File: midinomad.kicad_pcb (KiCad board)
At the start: 2 copper layers, 169.1 x 87.3 mm, 56 parts, among them J1 MIDI IN, J2 MIDI OUT, J3 Nomad 45, 55, J7 DC IN, U1 6N138, U2 L7805, U3 74HC4053

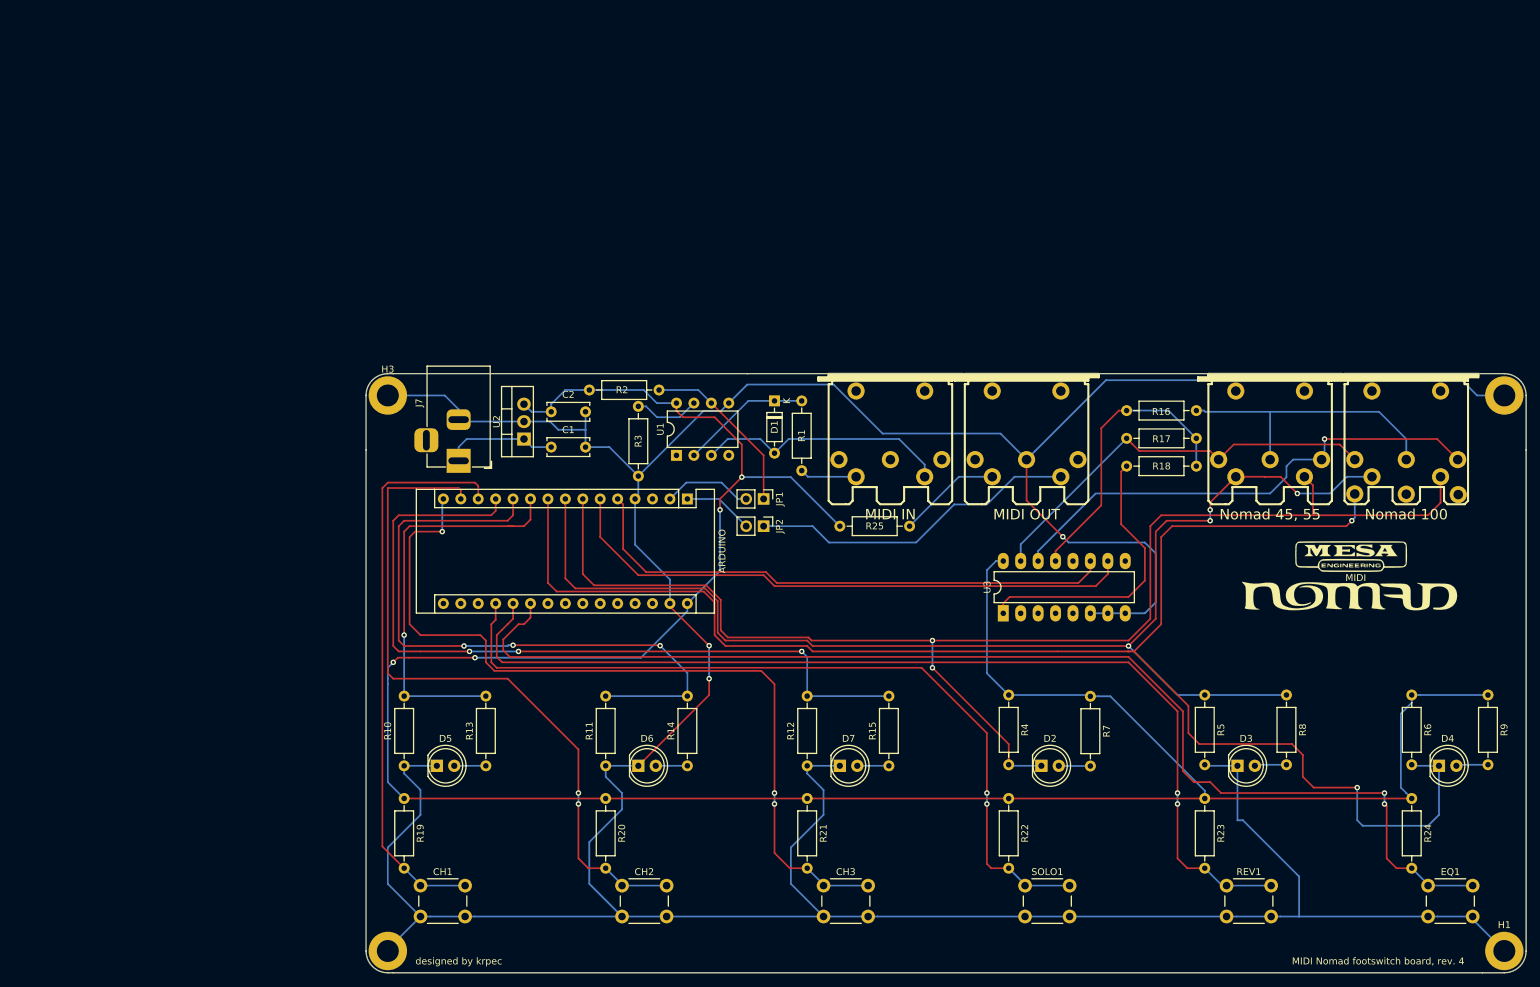
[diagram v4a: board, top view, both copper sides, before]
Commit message: Updated both schematics & PCB, added second 74hc4053.
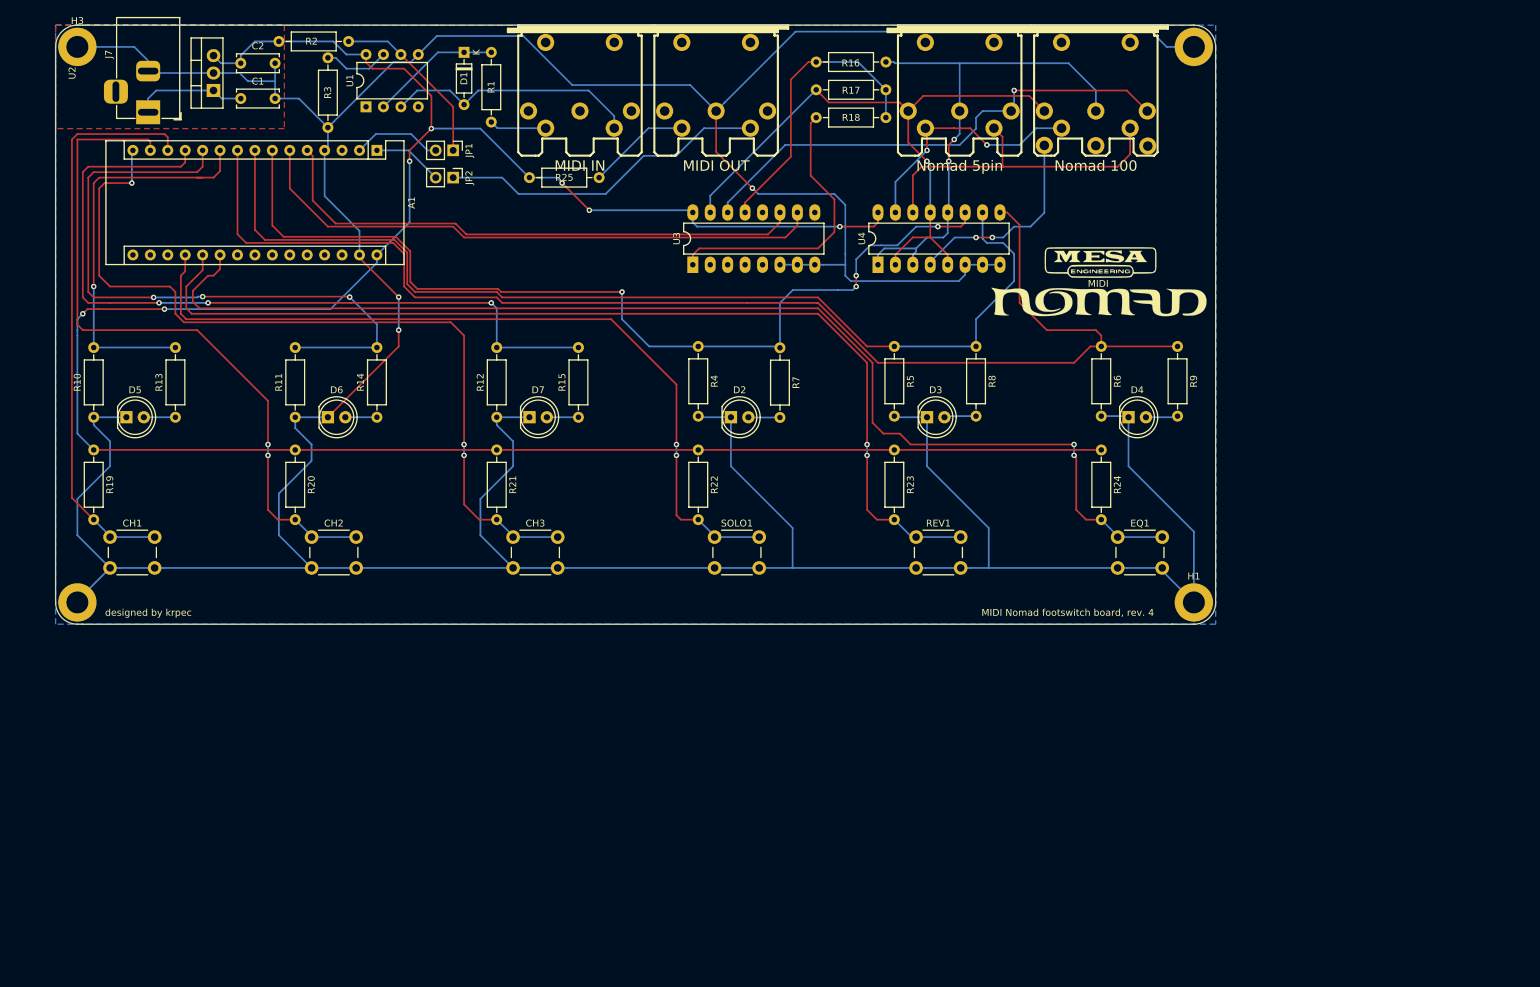
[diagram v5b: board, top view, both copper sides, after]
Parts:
- removed ARDUINO: Arduino_Nano_v3.x, Module:Arduino_Nano
- removed the G*** at (208.8, 101.6)
- removed NOMAD 100: Nomad 100, midinomad:din-8
- added A1: Arduino_Nano_v3.x, Module:Arduino_Nano, F.Cu at (66.7, 40.5)
- added G***: LOGO, midinomad-mux:board-logo, F.Cu at (172.2, 58.7)
- added J4: Nomad 100, midinomad:din-8, F.Cu at (171.4, 31.8)
- added U4: 74HC4053, Package_DIP:DIP-16_W7.62mm_LongPads, F.Cu at (139.7, 57.1)
- J3: value Nomad 45, 55 -> Nomad 5pin
- moved D1 68.0 mm to (79.4, 26.2)
- moved D2 68.0 mm to (118.3, 79.4)
- moved D3 68.0 mm to (146.8, 79.4)
- moved D4 68.0 mm to (176.2, 79.4)
- moved D5 68.0 mm to (30.2, 79.4)
- moved D6 68.0 mm to (59.5, 79.4)
- moved D7 68.0 mm to (88.9, 79.4)
- moved H3 68.0 mm to (23.0, 25.4)
- moved R1 68.0 mm to (83.3, 26.2)
- moved R10 68.0 mm to (25.4, 79.4)
- moved R11 68.0 mm to (54.8, 79.4)
- moved R12 68.0 mm to (84.1, 79.4)
- moved R13 68.0 mm to (37.3, 79.4)
- moved R14 68.0 mm to (66.7, 79.4)
- moved R15 68.0 mm to (96.0, 79.4)
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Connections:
- D2 pad 1: Arduino_D4 -> GNDREF
- D4 pad 1: Arduino_D6 -> GNDREF
- J3 pad 4: Arduino_D5 -> MESA_SWB_(REV)
- J3 pad 5: Arduino_D4 -> MESA_SWA_(SOLO)
- R4 pad 1: +5V -> Arduino_D4
- R4 pad 2: Arduino_D4 -> GNDREF
- R6 pad 1: +5V -> Arduino_D6
- R6 pad 2: Arduino_D6 -> GNDREF
- R7 pad 1: +5V -> Arduino_D4
- R9 pad 1: +5V -> Arduino_D6
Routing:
- net GNDREF: track 578.0 -> 670.5 mm
- net Arduino_D4: track 196.3 -> 139.4 mm, vias 2 -> 4
- net MESA_SWA_(SOLO): track 0.00 -> 48.3 mm
- net Arduino_D6: track 229.7 -> 191.4 mm, vias 2 -> 0
- net MESA_SWB_(REV): track 0.00 -> 36.1 mm, vias 0 -> 2
- net +2V: track 42.3 -> 76.3 mm, vias 0 -> 2
- net -3V: track 60.6 -> 93.0 mm, vias 0 -> 1
- net Arduino_D5: track 183.1 -> 151.5 mm, vias 4 -> 0
- net +5V: track 383.2 -> 353.2 mm, vias 4 -> 7
- net MESA_SWC_(EQ): track 0.00 -> 29.8 mm, vias 0 -> 2
- added copper zone on B.Cu, net GNDREF
- added copper zone on F.Cu, net GNDREF

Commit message: schematics changes
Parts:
- removed G***: LOGO, midinomad-mux:board-logo
- added C3: 0.1uF, Capacitor_THT:C_Disc_D6.0mm_W2.5mm_P5.00mm, F.Cu at (74.6, 48.4)
- added C4: 0.1uF, Capacitor_THT:C_Disc_D6.0mm_W2.5mm_P5.00mm, F.Cu at (108.7, 50.8)
- added C5: 0.1uF, Capacitor_THT:C_Disc_D6.0mm_W2.5mm_P5.00mm, F.Cu at (136.5, 49.8)
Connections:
- J7 pad 1: Net-(C1-Pad1) -> GNDREF
- J7 pad 2: GNDREF -> Net-(C1-Pad1)
- U4 pad 3: +2V -> -3V
- U4 pad 5: -3V -> +2V
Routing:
- net GNDREF: track 670.5 -> 712.6 mm
- net +2V: track 76.3 -> 87.7 mm
- net +5V: track 353.2 -> 361.3 mm
- net -3V: track 93.0 -> 90.5 mm
- net Net-(C1-Pad1): track 16.5 -> 17.1 mm

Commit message: Rev. 6 PCB & schematics
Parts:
- removed C4, C5: 0.1uF, Capacitor_THT:C_Disc_D6.0mm_W2.5mm_P5.00mm
- removed the U4 at (139.7, 57.1)
- added D10: LED, LED_THT:LED_D5.0mm, F.Cu at (220.7, 111.1)
- added D2: 1N4007, Diode_THT:D_DO-41_SOD81_P10.16mm_Horizontal, F.Cu at (169.9, 96.0)
- added D3: 1N4007, Diode_THT:D_DO-41_SOD81_P10.16mm_Horizontal, F.Cu at (194.5, 96.0)
- added G***: LOGO, midinomad-mux:board-logo, F.Cu at (122.2, 89.7)
- added K1: SANYOU_SRD_Form_C, Relay_THT:Relay_SPDT_SANYOU_SRD_Series_Form_C, F.Cu at (174.6, 92.1)
- added K2: SANYOU_SRD_Form_C, Relay_THT:Relay_SPDT_SANYOU_SRD_Series_Form_C, F.Cu at (199.2, 92.1)
- added K3: SANYOU_SRD_Form_C, Relay_THT:Relay_SPDT_SANYOU_SRD_Series_Form_C, F.Cu at (223.8, 92.1)
- added Q1: 2N2222, Package_TO_SOT_THT:TO-18-3, F.Cu at (162.7, 94.5)
- added Q2: 2N2222, Package_TO_SOT_THT:TO-18-3, F.Cu at (211.9, 94.5)
- added Q3: 2N2222, Package_TO_SOT_THT:TO-18-3, F.Cu at (187.3, 94.5)
- added R12: 220R, Resistor_THT:R_Axial_DIN0207_L6.3mm_D2.5mm_P10.16mm_Horizontal, F.Cu at (129.4, 77.8)
- added R2: 1k, Resistor_THT:R_Axial_DIN0207_L6.3mm_D2.5mm_P10.16mm_Horizontal, F.Cu at (154.8, 100.8)
- added R27: 10k, Resistor_THT:R_Axial_DIN0207_L6.3mm_D2.5mm_P10.16mm_Horizontal, F.Cu at (216.7, 100.8)
- added R28: 220R, Resistor_THT:R_Axial_DIN0207_L6.3mm_D2.5mm_P10.16mm_Horizontal, F.Cu at (227.8, 100.8)
- added R8: 1k, Resistor_THT:R_Axial_DIN0207_L6.3mm_D2.5mm_P10.16mm_Horizontal, F.Cu at (183.4, 100.8)
- added REF**: Symbol_GNU-GPL_CopperTop_Small, Symbol:Symbol_GNU-GPL_CopperTop_Small, F.Cu at (149.2, 131.8)
- added REF**: Polarity_Center_Negative_6mm_SilkScreen, Symbol:Polarity_Center_Negative_6mm_SilkScreen, F.Cu at (67.7, 66.5)
- added REF**: OSHW-Logo2_7.3x6mm_SilkScreen, Symbol:OSHW-Logo2_7.3x6mm_SilkScreen, F.Cu at (73.8, 131.8)
- added U2: MOC3041M, Package_DIP:DIP-6_W7.62mm_LongPads, F.Cu at (137.3, 74.6)
- D4: value LED -> 1N4007; footprint LED_THT:LED_D5.0mm -> Diode_THT:D_DO-41_SOD81_P10.16mm_Horizontal
- R6: value 10k -> 1k
- U3: value 74HC4053 -> MOC3041M; footprint Package_DIP:DIP-16_W7.62mm_LongPads -> Package_DIP:DIP-6_W7.62mm_LongPads
- moved R13 65.6 mm to (81.0, 119.1), turned to 180 degrees
- moved R14 65.6 mm to (169.1, 119.1), turned to 180 degrees
- moved R17 65.6 mm to (110.3, 119.1), turned to 180 degrees
- moved R18 65.6 mm to (197.6, 119.1), turned to 180 degrees
- moved R23 65.6 mm to (139.7, 119.1), turned to 180 degrees
- moved R24 65.0 mm to (227.0, 119.1), turned to 180 degrees
- moved R15 54.6 mm to (158.0, 100.8)
- moved R16 54.6 mm to (169.9, 101.0)
- moved D5 54.6 mm to (162.7, 111.1)
- moved D8 54.6 mm to (104.0, 111.1)
- moved R25 54.6 mm to (111.1, 111.1)
- moved R26 54.6 mm to (99.2, 111.1)
- moved R29 54.6 mm to (140.5, 111.1)
- moved R30 54.6 mm to (128.6, 111.1)
- moved D6 54.6 mm to (74.6, 111.1)
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- renumbered D2 to D5, D5 to D6, D3 to D7, D6 to D8, D7 to D9, J3 to J2, J4 to J3, J2 to J4, J7 to J5, R17 to R10, R18 to R11, R19 to R13, R22 to R14, R4 to R15, R7 to R16, R20 to R17, R23 to R18, R13 to R19, R10 to R20, R5 to R21, R8 to R22, R21 to R23, R14 to R25, R11 to R26, R15 to R29, R2 to R3, R12 to R30, R3 to R4, R25 to R5, R16 to R7, JP1 to RXJ1, JP2 to TXJ1, U2 to U4
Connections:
- D4 pad 1: GNDREF -> +5V
- R10 pad 2: Net-(R16-Pad1) -> Net-(R10-Pad2)
- R11 pad 1: Net-(R18-Pad1) -> Net-(R11-Pad1)
- R11 pad 2: Net-(R16-Pad1) -> Net-(R10-Pad2)
- R6 pad 1: Arduino_D6 -> Net-(Q2-Pad2)
- R6 pad 2: GNDREF -> Arduino_D6
- R7 pad 1: Net-(R16-Pad1) -> Net-(R10-Pad2)
- R9 pad 1: Arduino_D6 -> Net-(R9-Pad1)
- R9 pad 2: Net-(D4-Pad2) -> Arduino_D2
- U3 pad 1: Net-(R18-Pad1) -> Net-(R12-Pad1)
- U3 pad 2: Net-(U3-Pad2) -> GNDREF
- U3 pad 4: Net-(U3-Pad4) -> -3V
- U3 pad 6: GNDREF -> Net-(R11-Pad1)
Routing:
- net GNDREF: track 712.6 -> 520.5 mm, vias 3 -> 0
- net +5V: track 361.3 -> 417.4 mm, vias 7 -> 9
- net Arduino_D3: track 85.1 -> 29.9 mm
- net Arduino_D2: track 80.0 -> 26.2 mm
- net Net-(R10-Pad2): track 0.00 -> 52.3 mm
- net Net-(R16-Pad1): track 42.8 -> 0.00 mm
- net Net-(R18-Pad1): track 41.9 -> 0.00 mm
- net -3V: track 90.5 -> 53.0 mm, vias 1 -> 0
- net Net-(R11-Pad1): track 0.00 -> 37.0 mm
- net Net-(D2-Pad2): track 0.00 -> 26.0 mm
- net Net-(D3-Pad2): track 0.00 -> 26.0 mm
- net MESA_SWA_(SOLO): track 48.3 -> 73.4 mm, vias 0 -> 2
- net Net-(D4-Pad2): track 4.89 -> 26.1 mm
- net MESA_VCH: track 73.0 -> 94.1 mm, vias 1 -> 0
- net MESA_SWB_(REV): track 36.1 -> 55.9 mm, vias 2 -> 1
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- added copper zone on B.Cu, net -3V
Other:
- board text added: "MIDI Nomad footswitch board, rev. 6 | github.com/krpec/MIDINomad"
- board text removed: "MIDI Nomad footswitch board, rev. 4"

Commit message: before adding the rest of relays
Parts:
- removed G***: LOGO, midinomad-mux:board-logo
- removed the REF** at (149.2, 131.8)
- removed the REF** at (67.7, 66.5)
- Q1, Q2, Q3: footprint Package_TO_SOT_THT:TO-18-3 -> Package_TO_SOT_THT:TO-92
- moved Q1 2.86 mm to (164.3, 96.8), turned to 90 degrees
- moved Q2 2.86 mm to (213.5, 96.8), turned to 90 degrees
- moved Q3 2.86 mm to (188.9, 96.8), turned to 90 degrees
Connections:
- A1 pad 16: Net-(A1-Pad16) -> (no net)
- A1 pad 17: Net-(A1-Pad17) -> (no net)
- A1 pad 18: Net-(A1-Pad18) -> (no net)
- A1 pad 22: Net-(A1-Pad22) -> (no net)
- A1 pad 23: Net-(A1-Pad23) -> (no net)
- A1 pad 24: Net-(A1-Pad24) -> (no net)
- A1 pad 25: Net-(A1-Pad25) -> (no net)
- A1 pad 26: Net-(A1-Pad26) -> (no net)
- A1 pad 27: Net-(A1-Pad27) -> (no net)
- A1 pad 28: Net-(A1-Pad28) -> (no net)
- A1 pad 3: Net-(A1-Pad3) -> (no net)
- J1 pad 1: Net-(J1-Pad1) -> (no net)
- J1 pad 2: Net-(J1-Pad2) -> (no net)
- J1 pad 3: Net-(J1-Pad3) -> (no net)
- J3 pad 7: Net-(J3-Pad7) -> (no net)
- J4 pad 1: Net-(J4-Pad1) -> (no net)
- J4 pad 3: Net-(J4-Pad3) -> (no net)
- U1 pad 1: Net-(U1-Pad1) -> (no net)
- U1 pad 4: Net-(U1-Pad4) -> (no net)
- U2 pad 3: Net-(U2-Pad3) -> (no net)
- U2 pad 5: Net-(U2-Pad5) -> (no net)
- U3 pad 3: Net-(U3-Pad3) -> (no net)
- U3 pad 5: Net-(U3-Pad5) -> (no net)
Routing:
- net GNDREF: track 520.5 -> 378.6 mm
- net Net-(D3-Pad2): track 26.0 -> 23.4 mm
- net Net-(D2-Pad2): track 26.0 -> 23.4 mm
- net Net-(D4-Pad2): track 26.1 -> 23.5 mm
- net Net-(Q1-Pad2): track 8.77 -> 10.4 mm
- net Net-(C1-Pad1): track 17.1 -> 15.6 mm
- net Net-(Q3-Pad2): track 7.13 -> 8.32 mm
- net MESA_SWB_(REV): track 55.9 -> 57.0 mm
- net Net-(Q2-Pad2): track 6.76 -> 5.76 mm
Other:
- net class Default: trace_width 0.25 -> 0.254
- net class Power added: clearance 0.2, trace_width 0.381, via_dia 0.8, via_drill 0.4
- board text removed: "MIDI"
